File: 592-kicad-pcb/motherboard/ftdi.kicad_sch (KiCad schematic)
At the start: 22 parts, among them J11 Conn_01x02_Female, U13 FT232H, U14 SN74LVC1G125DCKR, U15 SN74LVC1G125DCKR, Y3 CSTNE12M0GH5L000R0

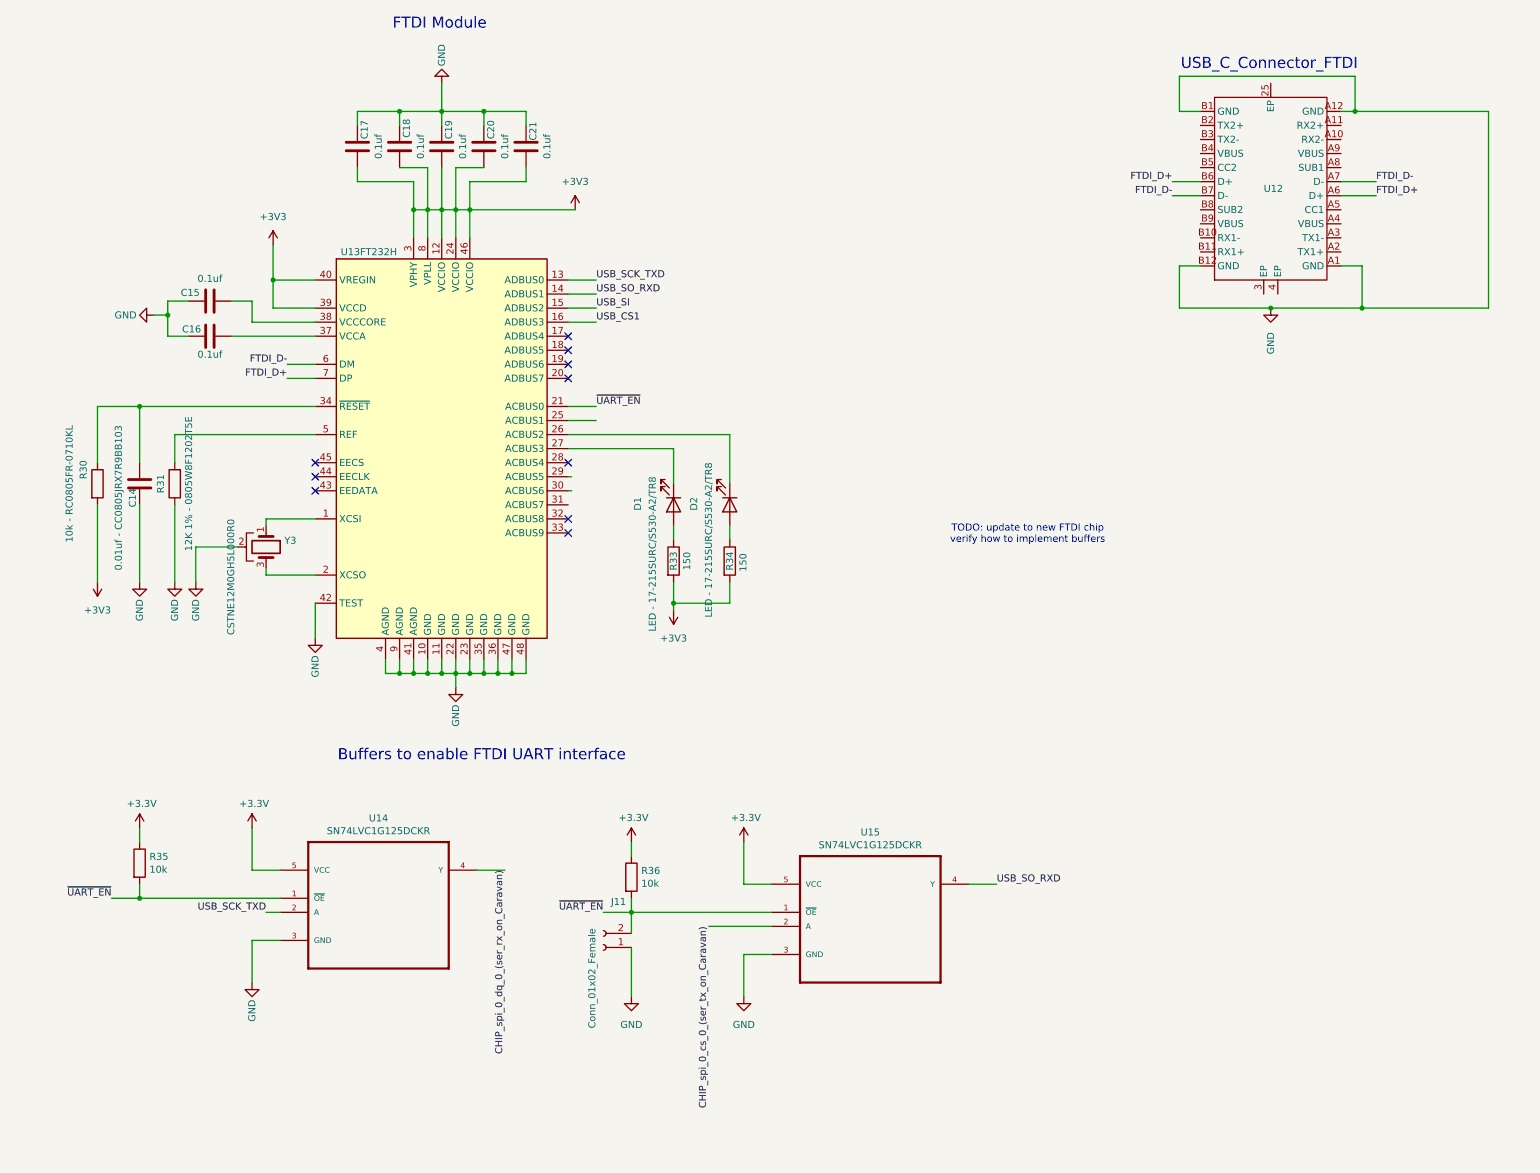
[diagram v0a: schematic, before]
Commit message: update ftdi chip
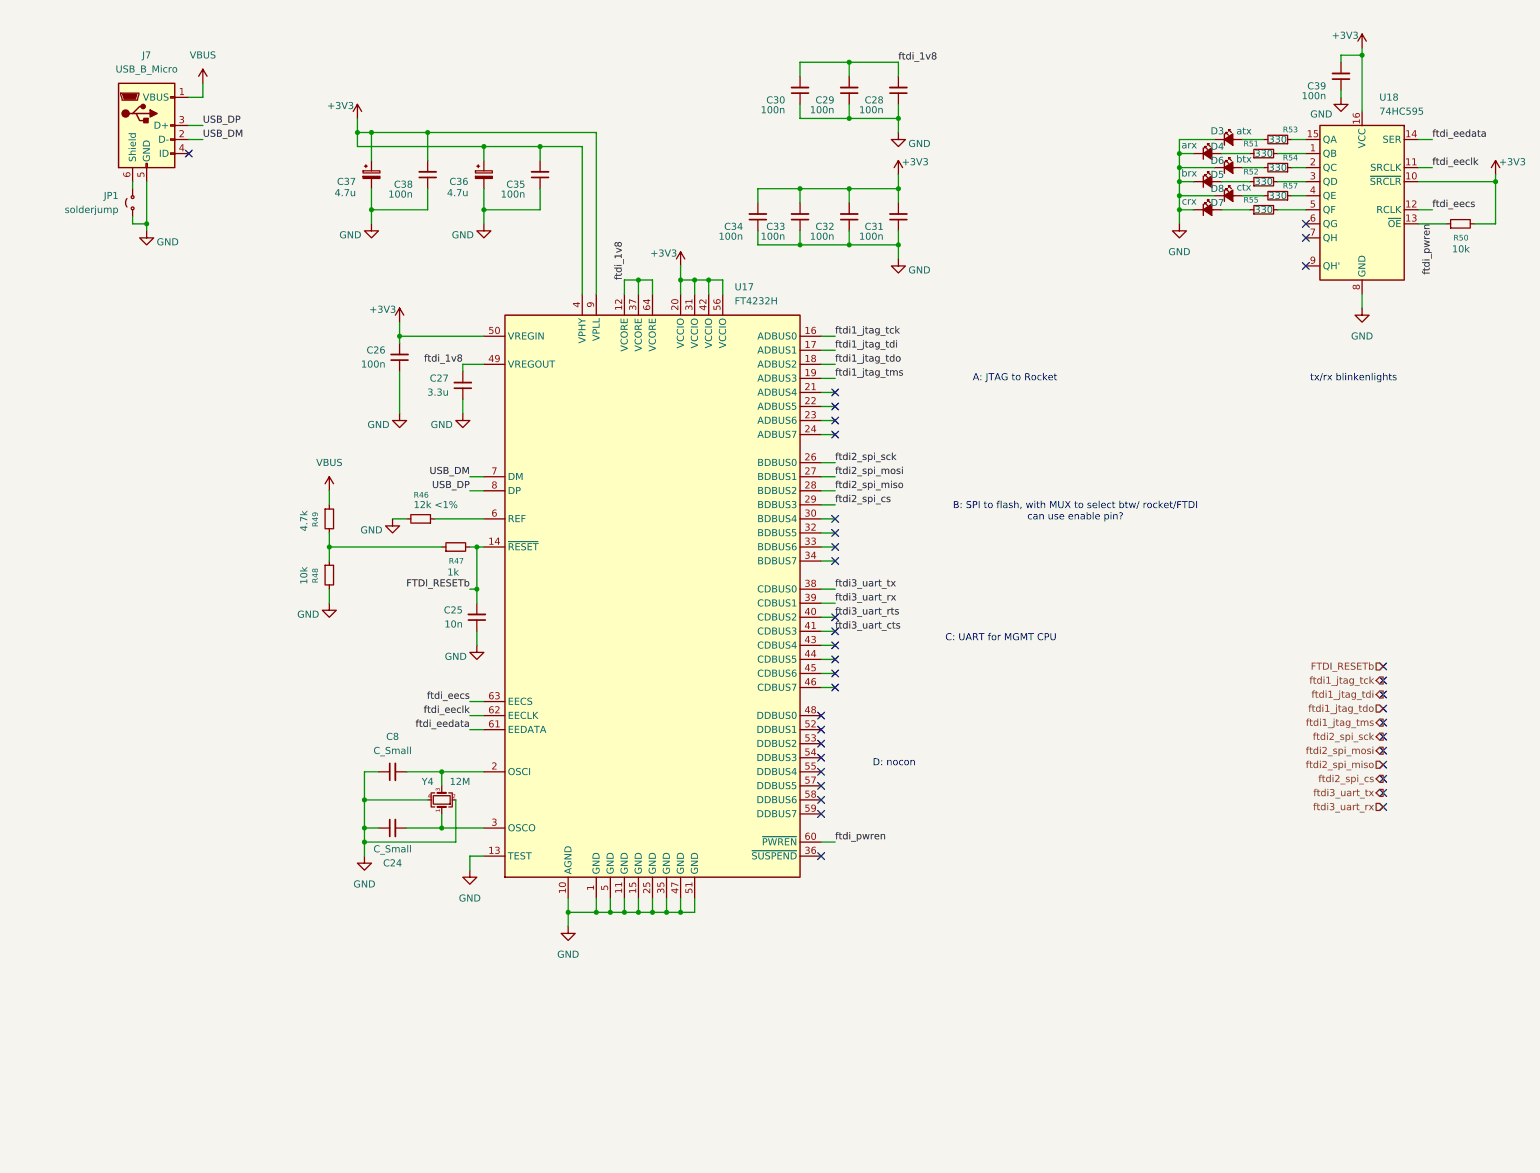
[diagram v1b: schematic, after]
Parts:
- removed C14: 0.01uf - CC0805JRX7R9BB103, Capacitor_SMD:C_0805_2012Metric, symbol Device:C
- removed C15, C16, C17, C18, C19, C20, C21: 0.1uf, Capacitor_SMD:C_0805_2012Metric, symbol Device:C
- removed D1, D2: LED - 17-215SURC/S530-A2/TR8, LED_SMD:LED_1206_3216Metric, symbol Device:LED
- removed J11: Conn_01x02_Female, Connector_PinHeader_2.54mm:PinHeader_1x02_P2.54mm_Vertical, symbol Connector:Conn_01x02_Female
- removed R30: 10k - RC0805FR-0710KL, Resistor_SMD:R_0805_2012Metric, symbol Device:R
- removed R31: 12K 1% - 0805W8F1202T5E, Resistor_SMD:R_0805_2012Metric, symbol Device:R
- removed R33, R34: 150, Resistor_SMD:R_0805_2012Metric, symbol Device:R
- removed R35, R36: 10k, Resistor_SMD:R_0805_2012Metric, symbol Device:R
- removed U12: ~, symbol New_Library:usb_C_Connector
- removed U13: FT232H, Package_DFN_QFN:QFN-48-1EP_8x8mm_P0.5mm_EP6.2x6.2mm, symbol Interface_USB:FT232H
- removed U14, U15: SN74LVC1G125DCKR, SOT65P210X110-5N, symbol Caravel_board:SN74LVC1G125DCKR
- removed Y3: CSTNE12M0GH5L000R0, strive_foot_prints:CSTNE12M0GH5L000R0, symbol Device:Crystal_GND2
- added C24, C8: C_Small, symbol Device:C_Small
- added C25: 10n, symbol Device:C_Small
- added C26, C28, C29, C30, C31, C32, C33, C34, C35, C38, C39: 100n, symbol Device:C_Small
- added C27: 3.3u, symbol Device:C_Small
- added C36, C37: 4.7u, symbol Device:C_Polarized_Small
- added D3: atx, symbol Device:LED_Small_Filled
- added D4: arx, symbol Device:LED_Small_Filled
- added D5: brx, symbol Device:LED_Small_Filled
- added D6: btx, symbol Device:LED_Small_Filled
- added D7: crx, symbol Device:LED_Small_Filled
- added D8: ctx, symbol Device:LED_Small_Filled
- added J7: USB_B_Micro, symbol Connector:USB_B_Micro
- added JP1: solderjump, symbol Jumper:Jumper_2_Small_Open
- added R46: 12k <1%, symbol Device:R_Small
- added R47: 1k, symbol Device:R_Small
- added R48, R50: 10k, symbol Device:R_Small
- added R49: 4.7k, symbol Device:R_Small
- added R51, R52, R53, R54, R55, R57: 330, symbol Device:R_Small
- added U17: FT4232H, symbol Interface_USB:FT4232H
- added U18: 74HC595, symbol 74xx:74HC595
- added Y4: 12M, Crystal:Crystal_SMD_3225-4Pin_3.2x2.5mm, symbol Device:Crystal_GND24_Small
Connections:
- net +3V3: now also C26.2, C31.2, C32.2, C33.2, C34.2, C35.2, C36.1, C37.1, C38.2, C39.2, R50.2, U17.20 (VCCIO), U17.31 (VCCIO), U17.4 (VPHY), U17.42 (VCCIO), U17.50 (VREGIN), U17.56 (VCCIO), U17.9 (VPLL), U18.10 (~{SRCLR}), U18.16 (VCC)
- net GND: now also C24.1, C25.1, C26.1, C27.1, C28.1, C29.1, C30.1, C31.1, C32.1, C33.1, C34.1, C35.1, C36.2, C37.2, C38.1, C39.1, C8.1, D3.1 (K), D4.1 (K), D5.1 (K), D6.1 (K), D7.1 (K), D8.1 (K), J7.5 (GND), JP1.1 (A), R46.2, R48.2, U17.1 (GND), U17.10 (AGND), U17.11 (GND), U17.13 (TEST), U17.15 (GND), U17.25 (GND), U17.35 (GND), U17.47 (GND), U17.5 (GND), U17.51 (GND), U18.8 (GND), Y4.2, Y4.4
- new net: D4.2 (A), R51.1
- new net: D3.2 (A), R53.2
- new net: D6.2 (A), R54.2
- new net: C8.2, U17.2 (OSCI), Y4.3
- new net: J7.6 (Shield), JP1.2 (B)
- new net: R47.1, R48.1, R49.2
- new net: R51.2, U18.1 (QB)
- new net: C24.2, U17.3 (OSCO), Y4.1
- new net: R46.1, U17.6 (REF)
- new net: D8.2 (A), R57.2
- new net: D5.2 (A), R52.1
- new net: R52.2, U18.3 (QD)
- new net: R57.1, U18.4 (QE)
- new net: R54.1, U18.2 (QC)
- new net: D7.2 (A), R55.1
- new net: R55.2, U18.5 (QF)
- new net: R53.1, U18.15 (QA)
- new net FTDI_RESETb: C25.2, R47.2, U17.14 (~{RESET})
- new net USB_DM: J7.2 (D-), U17.7 (DM)
- new net USB_DP: J7.3 (D+), U17.8 (DP)
- new net VBUS: J7.1 (VBUS), R49.1
- new net ftdi1_jtag_tck: U17.16 (ADBUS0)
- new net ftdi1_jtag_tdi: U17.17 (ADBUS1)
- new net ftdi1_jtag_tdo: U17.18 (ADBUS2)
- new net ftdi1_jtag_tms: U17.19 (ADBUS3)
- new net ftdi2_spi_cs: U17.29 (BDBUS3)
- new net ftdi2_spi_miso: U17.28 (BDBUS2)
- new net ftdi2_spi_mosi: U17.27 (BDBUS1)
- new net ftdi2_spi_sck: U17.26 (BDBUS0)
- new net ftdi3_uart_cts: U17.41 (CDBUS3)
- new net ftdi3_uart_rts: U17.40 (CDBUS2)
- new net ftdi3_uart_rx: U17.39 (CDBUS1)
- new net ftdi3_uart_tx: U17.38 (CDBUS0)
- new net ftdi_1v8: C27.2, C28.2, C29.2, C30.2, U17.12 (VCORE), U17.37 (VCORE), U17.49 (VREGOUT), U17.64 (VCORE)
- new net ftdi_eeclk: U17.62 (EECLK), U18.11 (SRCLK)
- new net ftdi_eecs: U17.63 (EECS), U18.12 (RCLK)
- new net ftdi_eedata: U17.61 (EEDATA), U18.14 (SER)
- new net ftdi_pwren: R50.1, U17.60 (~{PWREN}), U18.13 (~{OE})
- no-connect marks 10 -> 38
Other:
- note added: "A: JTAG to Rocket"
- note added: "B: SPI to flash, with MUX to select btw/ rocket/FTDI can use enable pin?"
- note added: "C: UART for MGMT CPU"
- note added: "D: nocon"
- note added: "tx/rx blinkenlights"
- note removed: "Buffers to enable FTDI UART interface"
- note removed: "FTDI Module"
- note removed: "TODO: update to new FTDI chip verify how to implement buffers"
- note removed: "USB_C_Connector_FTDI"

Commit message: combine hierarchy of all sans power
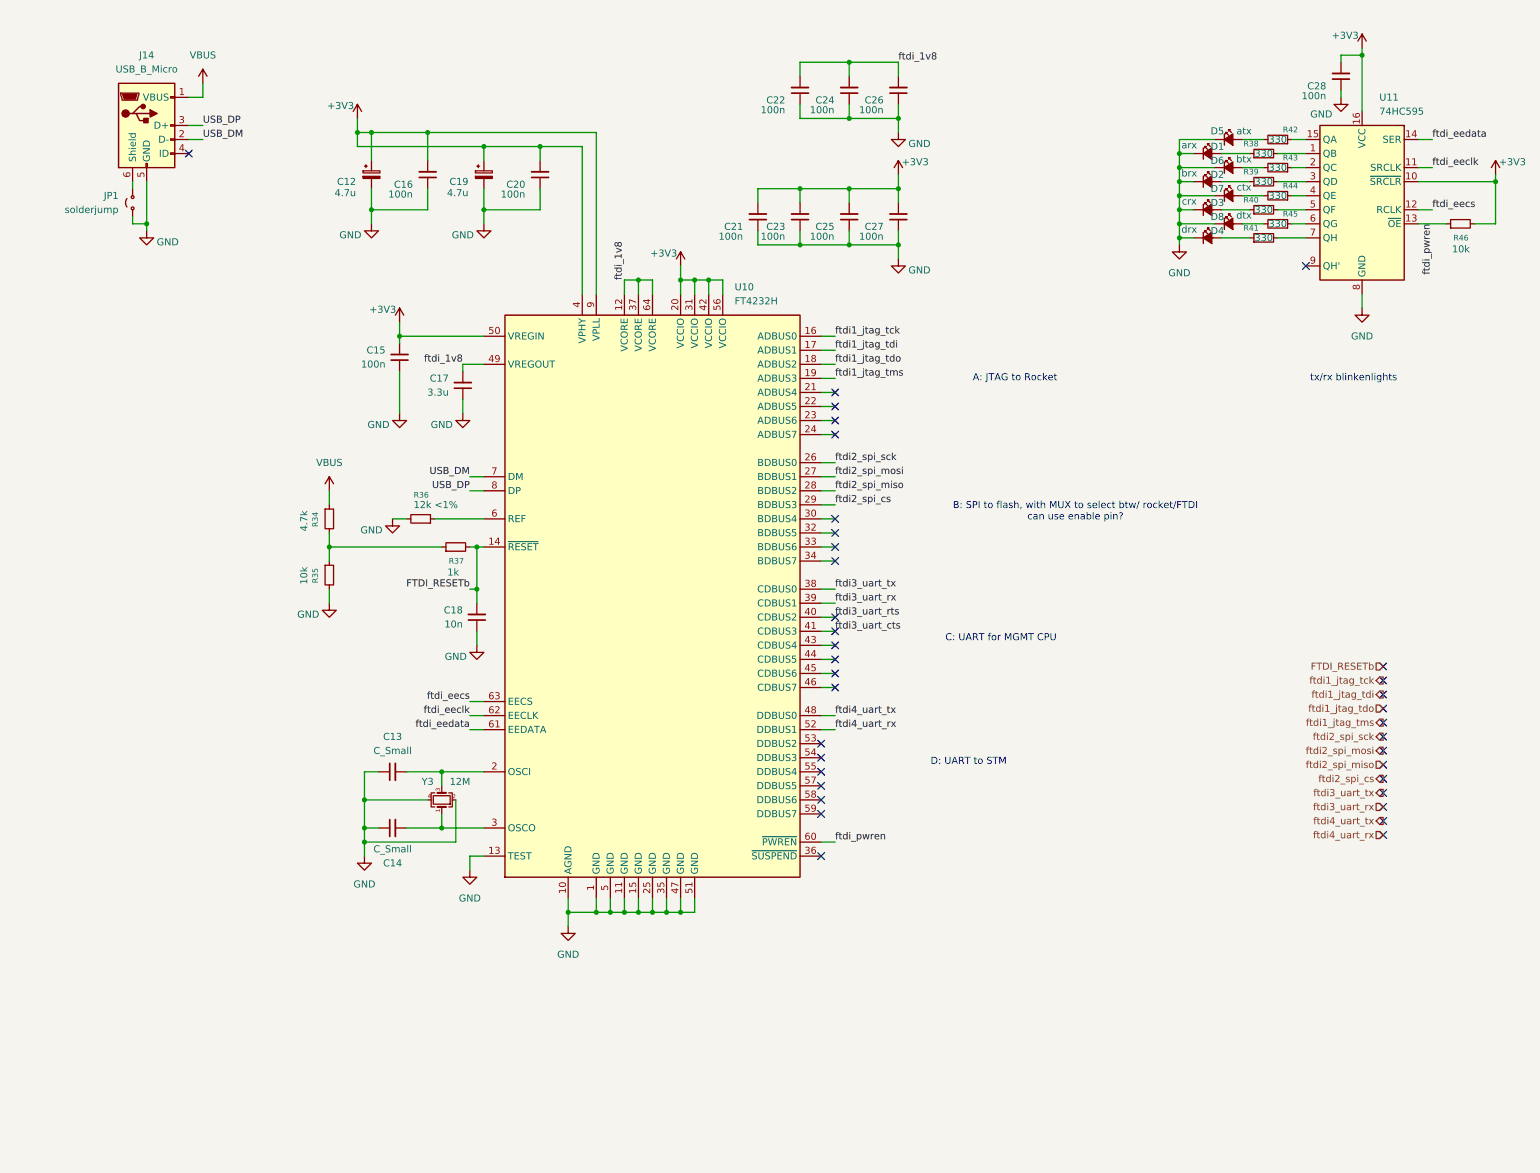
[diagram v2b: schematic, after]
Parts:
- added D4: drx, symbol Device:LED_Small_Filled
- added D8: dtx, symbol Device:LED_Small_Filled
- added R41, R45: 330, symbol Device:R_Small
- renumbered C37 to C12, C8 to C13, C24 to C14, C26 to C15, C38 to C16, C27 to C17, C25 to C18, C36 to C19, C35 to C20, C34 to C21, C30 to C22, C33 to C23, C29 to C24, C32 to C25, C28 to C26, C31 to C27, C39 to C28, D4 to D1, D5 to D2, D7 to D3, D3 to D5, D8 to D7, J7 to J14, R49 to R34, R48 to R35, R46 to R36, R47 to R37, R51 to R38, R52 to R39, R55 to R40, R53 to R42, R54 to R43, R57 to R44, R50 to R46, U17 to U10, U18 to U11, Y4 to Y3
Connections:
- net GND: now also D4.1 (K), D8.1 (K)
- net ftdi4_uart_tx: now reaches U10.48 (DDBUS0)
- net ftdi4_uart_rx: now reaches U10.52 (DDBUS1)
- net at U11.6 (QG): now also R45.1
- net at U11.7 (QH): now also R41.2
- new net: D8.2 (A), R45.2
- new net: D4.2 (A), R41.1
- no-connect marks 38 -> 36
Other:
- note added: "D: UART to STM"
- note removed: "D: nocon"

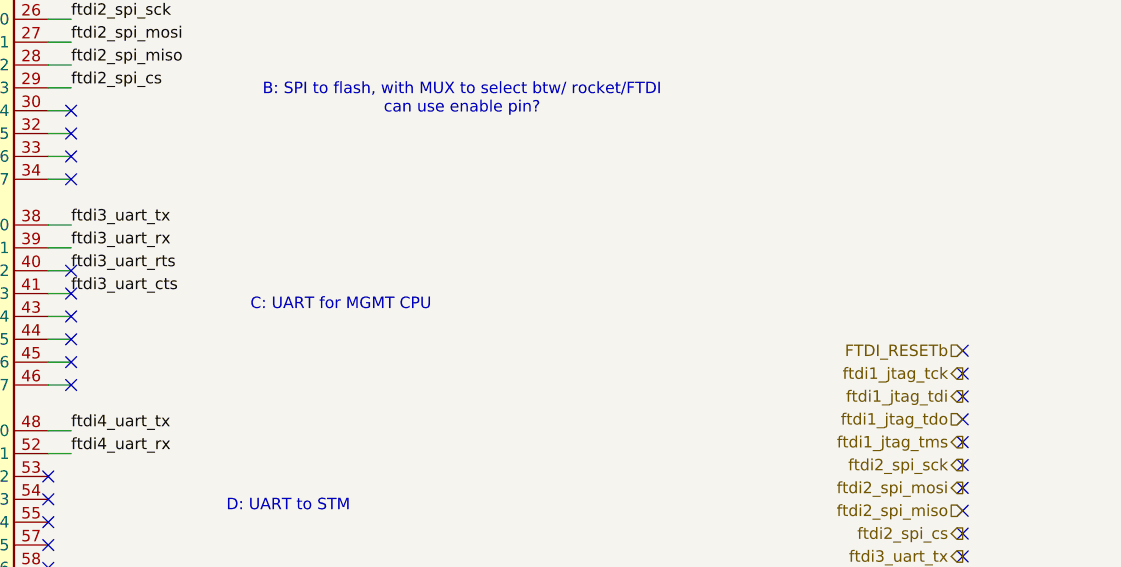
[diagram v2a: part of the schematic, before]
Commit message: partial update to use STM board, updated muxing of FTDI
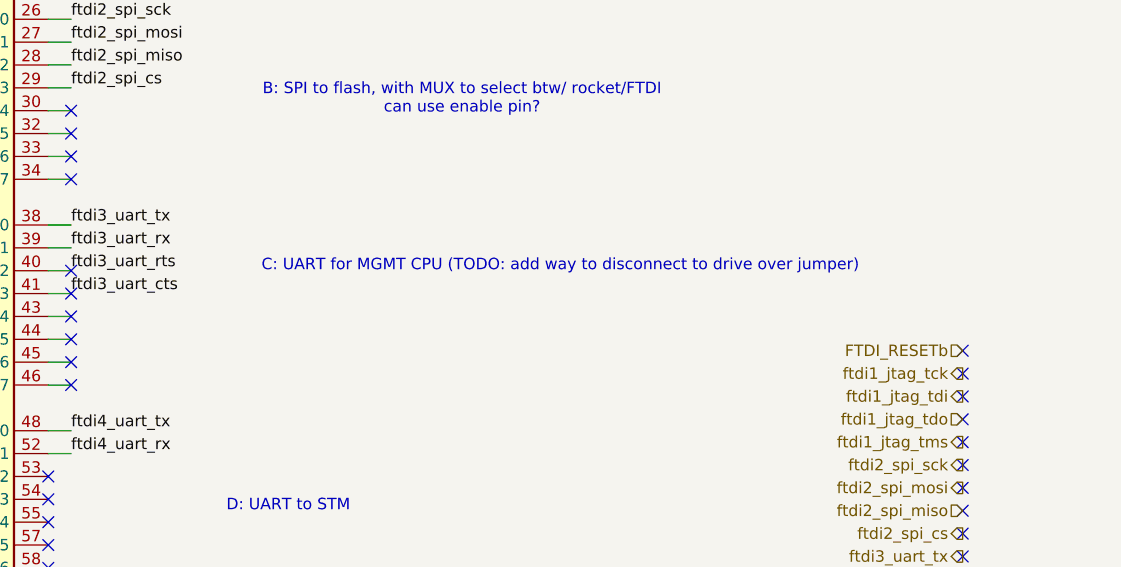
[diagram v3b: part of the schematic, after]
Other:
- note added: "C: UART for MGMT CPU (TODO: add way to disconnect to drive over jumper)"
- note removed: "C: UART for MGMT CPU"
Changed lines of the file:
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@@
 		)
 	)
-	(text "C: UART for MGMT CPU"
+	(text "C: UART for MGMT CPU (TODO: add way to disconnect to drive over jumper)"
 		(exclude_from_sim no)
-		(at 187.452 124.46 0)
+		(at 211.836 120.142 0)
 		(effects
 			(font
